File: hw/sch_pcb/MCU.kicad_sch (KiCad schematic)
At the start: 30 parts, among them P1 Conn_01x06, P2 Conn_01x06, P3 Conn_01x06, U1 STM32F405RGT6, X1 ABM3B-8.000MHZ

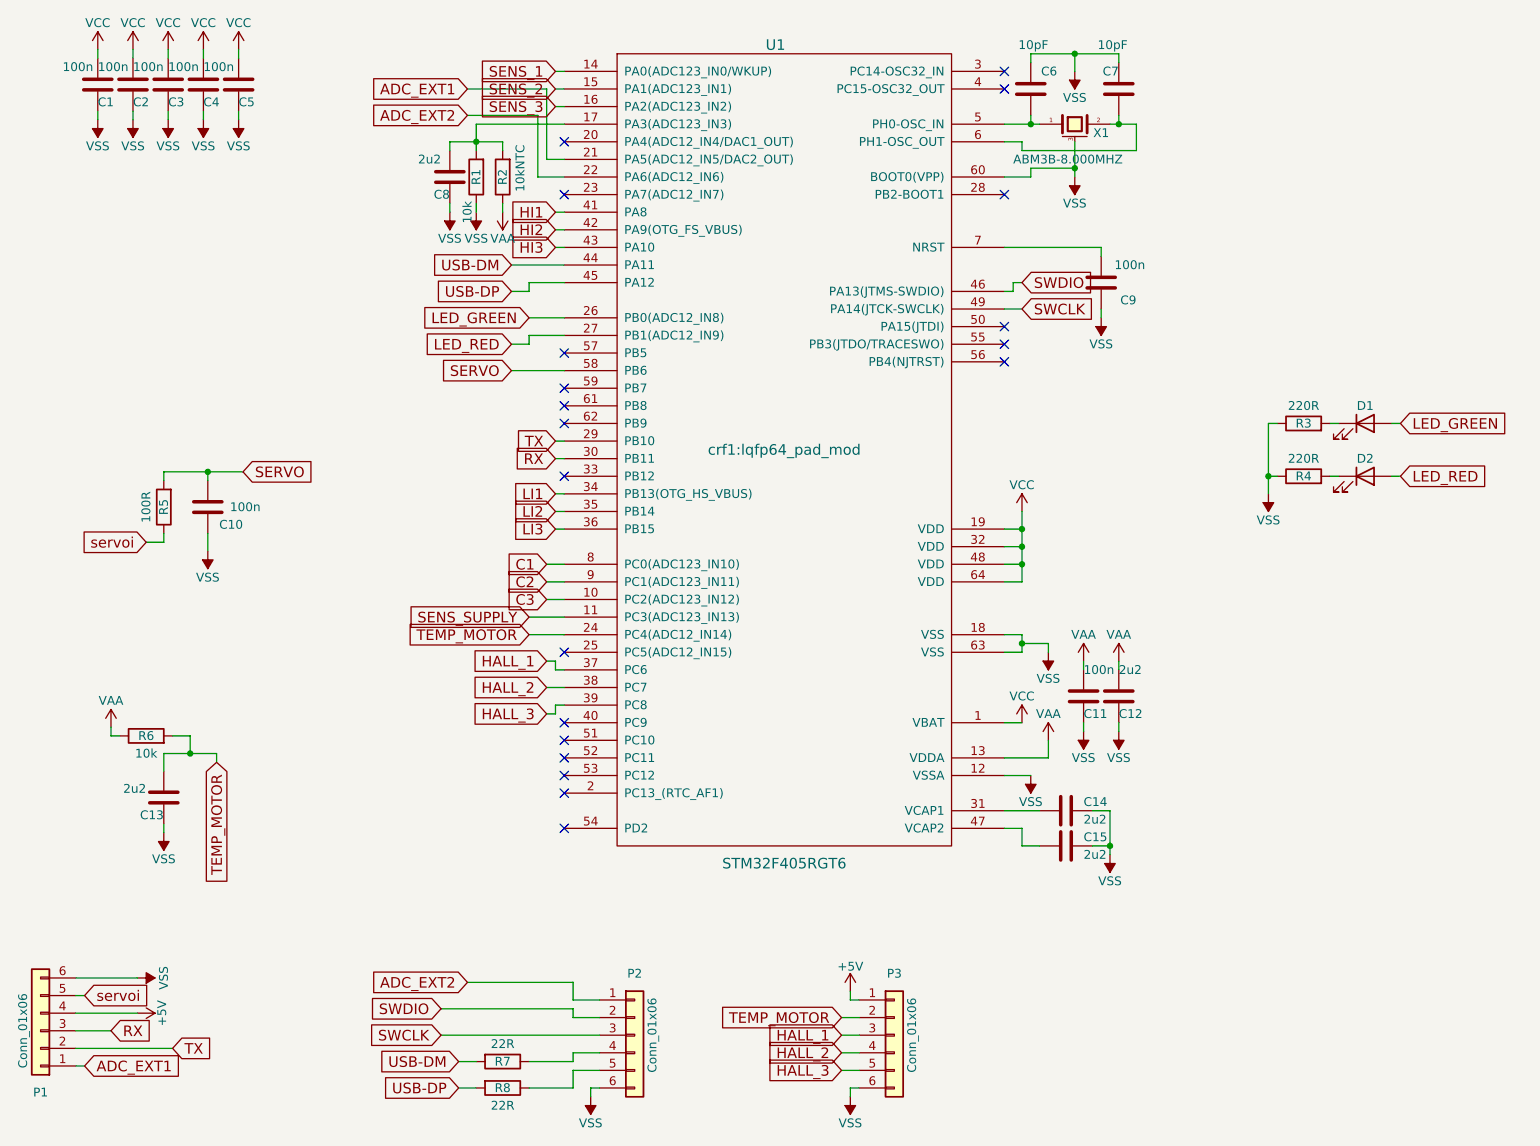
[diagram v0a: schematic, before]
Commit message: CAN interface connector added #3
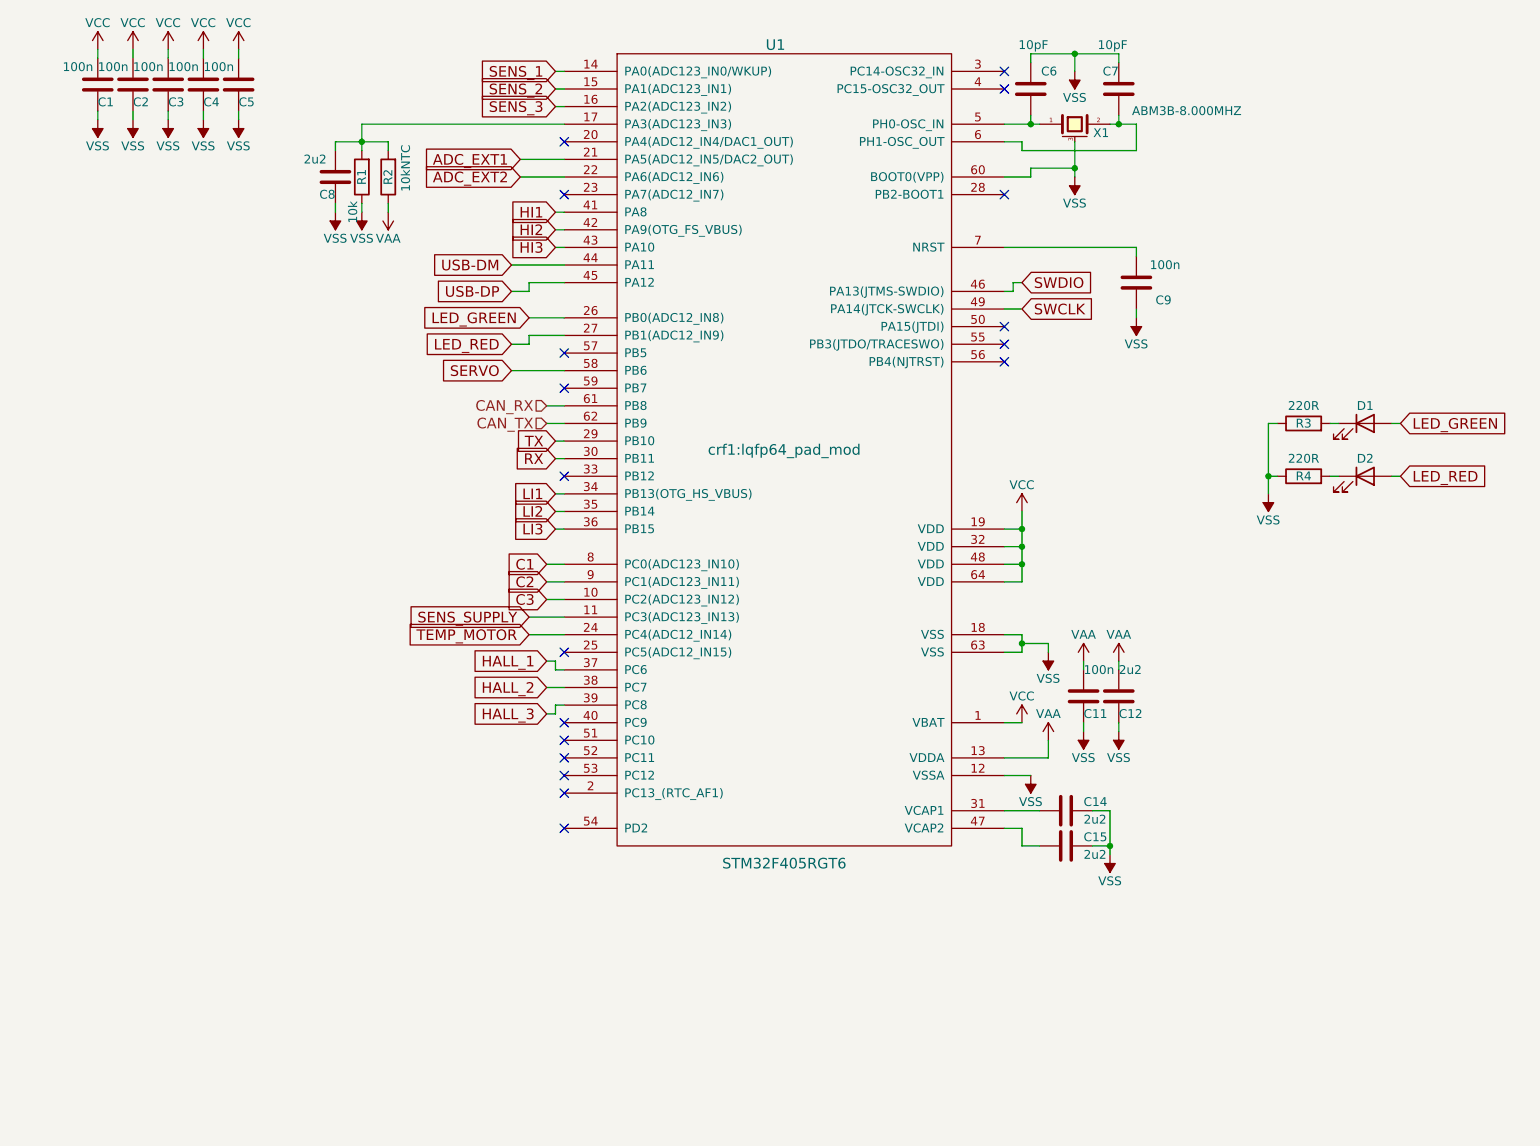
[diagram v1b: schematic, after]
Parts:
- removed C10: 100n, Resistors_SMD:R_0603, symbol Device:C
- removed C13: 2u2, Capacitors_SMD:C_0603, symbol Device:C
- removed P1, P2, P3: Conn_01x06, kicad_subory:JST_ZH_1.5_6-Pin, symbol Connector_Generic:Conn_01x06
- removed R5: 100R, Resistors_SMD:R_0603, symbol Device:R
- removed R6: 10k, Resistors_SMD:R_0603, symbol Device:R
- removed R7, R8: 22R, Resistors_SMD:R_0603, symbol Device:R
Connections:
- net CAN_RX: now reaches U1.61 (PB8)
- net CAN_TX: now reaches U1.62 (PB9)
- no-connect marks 20 -> 18
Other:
- moved on the sheet: C8, C9, R1, R2
